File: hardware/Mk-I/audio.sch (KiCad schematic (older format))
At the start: 9 parts, among them U5 SGTL5000

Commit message: Cleanup schematics
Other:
- moved on the sheet: C10, C11, HP_OUT1, LINE_IN1, U5
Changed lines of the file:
@@
 Comment4 ""
 $EndDescr
-Text GLabel 5150 2900 0    60   Input ~ 0
+Text GLabel 4500 3300 0    60   Input ~ 0
 Audio_SDA
-Text GLabel 5150 3050 0    60   Input ~ 0
+Text GLabel 4500 3450 0    60   Input ~ 0
 Audio_SCL
-Text GLabel 5150 3300 0    60   Input ~ 0
+Text GLabel 4500 3700 0    60   Input ~ 0
 I2S_MCLK
-Text GLabel 5150 3450 0    60   Input ~ 0
+Text GLabel 4500 3850 0    60   Input ~ 0
 I2S_SCLK
-Text GLabel 5150 3600 0    60   Input ~ 0
+Text GLabel 4500 4000 0    60   Input ~ 0
 I2S_LRCLK
-Text GLabel 5150 3750 0    60   Input ~ 0
+Text GLabel 4500 4150 0    60   Input ~ 0
 I2S_DIN
-Text GLabel 5150 3900 0    60   Input ~ 0
+Text GLabel 4500 4300 0    60   Input ~ 0
 I2S_DOUT
-Text GLabel 5250 2050 0    60   Input ~ 0
+Text GLabel 4600 2450 0    60   Input ~ 0
 3V3
 Wire Wire Line
-	5150 4250 5100 4250
+	4500 4650 4450 4650
 Wire Wire Line
-	5100 4250 5100 4450
+	4450 4650 4450 4850
 $Comp
 L GND #PWR032
 U 1 1 585E79AD
-P 5100 4450
-F 0 "#PWR032" H 5100 4450 30  0001 C CNN
-F 1 "GND" H 5100 4380 30  0001 C CNN
-F 2 "" H 5100 4450 60  0001 C CNN
-F 3 "" H 5100 4450 60  0001 C CNN
-	1    5100 4450
+P 4450 4850
+F 0 "#PWR032" H 4450 4850 30  0001 C CNN
+F 1 "GND" H 4450 4780 30  0001 C CNN
+F 2 "" H 4450 4850 60  0001 C CNN
+F 3 "" H 4450 4850 60  0001 C CNN
+	1    4450 4850
 	1    0    0    -1
 $EndComp
@@
 L C C6
 U 1 1 585E7B78
-P 4750 4300
-F 0 "C6" H 4750 4400 40  0000 L CNN
-F 1 "0.1uF" H 4756 4215 40  0000 L CNN
-F 2 "Capacitors_SMD:C_0805" H 4788 4150 30  0001 C CNN
-F 3 "" H 4750 4300 60  0000 C CNN
-	1    4750 4300
+P 4100 4700
+F 0 "C6" H 4100 4800 40  0000 L CNN
+F 1 "0.1uF" H 4106 4615 40  0000 L CNN
+F 2 "Capacitors_SMD:C_0805" H 4138 4550 30  0001 C CNN
+F 3 "" H 4100 4700 60  0000 C CNN
+	1    4100 4700
 	1    0    0    -1
 $EndComp
@@
 L GND #PWR033
 U 1 1 585E7BA3
-P 4750 4500
-F 0 "#PWR033" H 4750 4500 30  0001 C CNN
-F 1 "GND" H 4750 4430 30  0001 C CNN
-F 2 "" H 4750 4500 60  0001 C CNN
-F 3 "" H 4750 4500 60  0001 C CNN
-	1    4750 4500
+P 4100 4900
+F 0 "#PWR033" H 4100 4900 30  0001 C CNN
+F 1 "GND" H 4100 4830 30  0001 C CNN
+F 2 "" H 4100 4900 60  0001 C CNN
+F 3 "" H 4100 4900 60  0001 C CNN
+	1    4100 4900
 	1    0    0    -1
 $EndComp
 Wire Wire Line
-	5150 4100 4750 4100
+	4500 4500 4100 4500
 Wire Wire Line
-	6400 3500 7375 3500
+	5750 3900 6725 3900
 Wire Wire Line
-	6400 3650 7375 3650
+	5750 4050 6725 4050
 $Comp
 L C C7
 U 1 1 585E8504
-P 5550 2300
-F 0 "C7" H 5550 2400 40  0000 L CNN
-F 1 "0.1uF" H 5556 2215 40  0000 L CNN
-F 2 "Capacitors_SMD:C_0805" H 5588 2150 30  0001 C CNN
-F 3 "" H 5550 2300 60  0000 C CNN
-	1    5550 2300
+P 4900 2700
+F 0 "C7" H 4900 2800 40  0000 L CNN
+F 1 "0.1uF" H 4906 2615 40  0000 L CNN
+F 2 "Capacitors_SMD:C_0805" H 4938 2550 30  0001 C CNN
+F 3 "" H 4900 2700 60  0000 C CNN
+	1    4900 2700
 	1    0    0    -1
 $EndComp
@@
 L C C8
 U 1 1 585E857A
-P 5800 2300
-F 0 "C8" H 5800 2400 40  0000 L CNN
-F 1 "0.1uF" H 5806 2215 40  0000 L CNN
-F 2 "Capacitors_SMD:C_0805" H 5838 2150 30  0001 C CNN
-F 3 "" H 5800 2300 60  0000 C CNN
-	1    5800 2300
+P 5150 2700
+F 0 "C8" H 5150 2800 40  0000 L CNN
+F 1 "0.1uF" H 5156 2615 40  0000 L CNN
+F 2 "Capacitors_SMD:C_0805" H 5188 2550 30  0001 C CNN
+F 3 "" H 5150 2700 60  0000 C CNN
+	1    5150 2700
 	1    0    0    -1
 $EndComp
@@
 L C C9
 U 1 1 585E859F
-P 6050 2300
-F 0 "C9" H 6050 2400 40  0000 L CNN
-F 1 "0.1uF" H 6056 2215 40  0000 L CNN
-F 2 "Capacitors_SMD:C_0805" H 6088 2150 30  0001 C CNN
-F 3 "" H 6050 2300 60  0000 C CNN
-	1    6050 2300
+P 5400 2700
+F 0 "C9" H 5400 2800 40  0000 L CNN
+F 1 "0.1uF" H 5406 2615 40  0000 L CNN
+F 2 "Capacitors_SMD:C_0805" H 5438 2550 30  0001 C CNN
+F 3 "" H 5400 2700 60  0000 C CNN
+	1    5400 2700
 	1    0    0    -1
 $EndComp
@@
 L SGTL5000 U5
 U 1 1 585E883F
-P 5400 2800
-F 0 "U5" H 5300 3050 60  0000 C CNN
-F 1 "SGTL5000" H 5750 1250 60  0000 C CNN
-F 2 "Housings_DFN_QFN:UQFN-20-1EP_3x3mm_Pitch0.4mm" H 5400 2750 60  0001 C CNN
-F 3 "" H 5400 2750 60  0001 C CNN
-	1    5400 2800
+P 4750 3200
+F 0 "U5" H 4650 3450 60  0000 C CNN
+F 1 "SGTL5000" H 5100 1650 60  0000 C CNN
+F 2 "Housings_DFN_QFN:UQFN-20-1EP_3x3mm_Pitch0.4mm" H 4750 3150 60  0001 C CNN
+F 3 "" H 4750 3150 60  0001 C CNN
+	1    4750 3200
 	1    0    0    -1
 $EndComp
 Wire Wire Line
-	6050 2100 6050 2050
+	5400 2500 5400 2450
 Wire Wire Line
-	6050 2050 5250 2050
+	5400 2450 4600 2450
 Wire Wire Line
-	5550 2100 5550 2050
-Connection ~ 5550 2050
+	4900 2500 4900 2450
+Connection ~ 4900 2450
 Wire Wire Line
-	5800 2100 5800 2050
-Connection ~ 5800 2050
+	5150 2500 5150 2450
+Connection ~ 5150 2450
 $Comp
 L Csmall C10
 U 1 1 585E8C6B
-P 6650 2900
-F 0 "C10" V 6700 2800 30  0000 L CNN
-F 1 "1uF" V 6700 2950 30  0000 L CNN
-F 2 "Capacitors_SMD:C_0805" H 6650 2900 60  0001 C CNN
-F 3 "" H 6650 2900 60  0000 C CNN
-	1    6650 2900
+P 6000 3300
+F 0 "C10" V 6050 3200 30  0000 L CNN
+F 1 "1uF" V 6050 3350 30  0000 L CNN
+F 2 "Capacitors_SMD:C_0805" H 6000 3300 60  0001 C CNN
+F 3 "" H 6000 3300 60  0000 C CNN
+	1    6000 3300
 	0    1    1    0
 $EndComp
@@
 L Csmall C11
 U 1 1 585E8E3F
-P 6650 3050
-F 0 "C11" V 6700 2950 30  0000 L CNN
-F 1 "1uF" V 6700 3100 30  0000 L CNN
-F 2 "Capacitors_SMD:C_0805" H 6650 3050 60  0001 C CNN
-F 3 "" H 6650 3050 60  0000 C CNN
-	1    6650 3050
+P 6000 3450
+F 0 "C11" V 6050 3350 30  0000 L CNN
+F 1 "1uF" V 6050 3500 30  0000 L CNN
+F 2 "Capacitors_SMD:C_0805" H 6000 3450 60  0001 C CNN
+F 3 "" H 6000 3450 60  0000 C CNN
+	1    6000 3450
 	0    1    1    0
 $EndComp
 Wire Wire Line
-	6550 2900 6400 2900
+	5900 3300 5750 3300
 Wire Wire Line
-	6550 3050 6400 3050
+	5900 3450 5750 3450
 Wire Wire Line
-	6750 2900 7375 2900
+	6100 3300 6725 3300
 Wire Wire Line
-	6750 3050 7375 3050
+	6100 3450 6725 3450
 $Comp
 L 3.5_audio_jack HP_OUT1
 U 1 1 5863AC9E
-P 7750 4025
-F 0 "HP_OUT1" H 7825 3400 60  0000 C CNN
-F 1 "3.5_audio_jack" H 7750 4025 60  0001 C CNN
-F 2 "POSS:lumberg_3.5_audio_jack_1503_02" H 7750 4025 60  0001 C CNN
-F 3 "" H 7750 4025 60  0001 C CNN
-	1    7750 4025
+P 7100 4425
+F 0 "HP_OUT1" H 7175 3800 60  0000 C CNN
+F 1 "3.5_audio_jack" H 7100 4425 60  0001 C CNN
+F 2 "POSS:lumberg_3.5_audio_jack_1503_02" H 7100 4425 60  0001 C CNN
+F 3 "" H 7100 4425 60  0001 C CNN
+	1    7100 4425
 	-1   0    0    1
 $EndComp
 Wire Wire Line
-	6400 3800 7375 3800
+	5750 4200 6725 4200
 $Comp
 L 3.5_audio_jack LINE_IN1
 U 1 1 5863B129
-P 7750 3425
-F 0 "LINE_IN1" H 7825 2800 60  0000 C CNN
-F 1 "3.5_audio_jack" H 7600 2800 60  0001 C CNN
-F 2 "POSS:lumberg_3.5_audio_jack_1503_02" H 7750 3425 60  0001 C CNN
-F 3 "" H 7750 3425 60  0001 C CNN
-	1    7750 3425
+P 7100 3825
+F 0 "LINE_IN1" H 7175 3200 60  0000 C CNN
+F 1 "3.5_audio_jack" H 6950 3200 60  0001 C CNN
+F 2 "POSS:lumberg_3.5_audio_jack_1503_02" H 7100 3825 60  0001 C CNN
+F 3 "" H 7100 3825 60  0001 C CNN
+	1    7100 3825
 	-1   0    0    1
 $EndComp
@@
 L GND #PWR034
 U 1 1 5863B3F7
-P 7325 3275
-F 0 "#PWR034" H 7325 3275 30  0001 C CNN
-F 1 "GND" H 7325 3205 30  0001 C CNN
-F 2 "" H 7325 3275 60  0001 C CNN
-F 3 "" H 7325 3275 60  0001 C CNN
-	1    7325 3275
+P 6675 3675
+F 0 "#PWR034" H 6675 3675 30  0001 C CNN
+F 1 "GND" H 6675 3605 30  0001 C CNN
+F 2 "" H 6675 3675 60  0001 C CNN
+F 3 "" H 6675 3675 60  0001 C CNN
+	1    6675 3675
 	1    0    0    -1
 $EndComp
 Wire Wire Line
-	7375 3200 7325 3200
+	6725 3600 6675 3600
 Wire Wire Line
-	7325 3200 7325 3275
+	6675 3600 6675 3675
 $EndSCHEMATC

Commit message: HW: Add a DFU mode switch
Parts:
- C6, C7, C8, C9: symbol C -> C-RESCUE-wnm_mk_1
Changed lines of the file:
@@
 EESchema Schematic File Version 2
+LIBS:wnm_mk_1-rescue
 LIBS:power
 LIBS:device
@@
 LIBS:microchip_pic12mcu
 LIBS:microchip_pic16mcu
-LIBS:microchip1
 LIBS:msp430
 LIBS:nxp_armmcu
@@
 LIBS:relays
 LIBS:sensors
-LIBS:special
 LIBS:stm8
 LIBS:stm32
@@
 	4450 4650 4450 4850
 $Comp
-L GND #PWR032
+L GND-RESCUE-wnm_mk_1 #PWR032
 U 1 1 585E79AD
 P 4450 4850
+AR Path="/585E79AD" Ref="#PWR032"  Part="1"
+AR Path="/585E4C2D/585E79AD" Ref="#PWR032"  Part="1"
 F 0 "#PWR032" H 4450 4850 30  0001 C CNN
 F 1 "GND" H 4450 4780 30  0001 C CNN
@@
 $EndComp
 $Comp
-L C C6
+L C-RESCUE-wnm_mk_1 C6
 U 1 1 585E7B78
 P 4100 4700
+AR Path="/585E7B78" Ref="C6"  Part="1"
+AR Path="/585E4C2D/585E7B78" Ref="C6"  Part="1"
 F 0 "C6" H 4100 4800 40  0000 L CNN
 F 1 "0.1uF" H 4106 4615 40  0000 L CNN
@@
 $EndComp
 $Comp
-L GND #PWR033
+L GND-RESCUE-wnm_mk_1 #PWR033
 U 1 1 585E7BA3
 P 4100 4900
+AR Path="/585E7BA3" Ref="#PWR033"  Part="1"
+AR Path="/585E4C2D/585E7BA3" Ref="#PWR033"  Part="1"
 F 0 "#PWR033" H 4100 4900 30  0001 C CNN
 F 1 "GND" H 4100 4830 30  0001 C CNN
@@
 	5750 4050 6725 4050
 $Comp
-L C C7
+L C-RESCUE-wnm_mk_1 C7
 U 1 1 585E8504
 P 4900 2700
+AR Path="/585E8504" Ref="C7"  Part="1"
+AR Path="/585E4C2D/585E8504" Ref="C7"  Part="1"
 F 0 "C7" H 4900 2800 40  0000 L CNN
 F 1 "0.1uF" H 4906 2615 40  0000 L CNN
@@
 $EndComp
 $Comp
-L C C8
+L C-RESCUE-wnm_mk_1 C8
 U 1 1 585E857A
 P 5150 2700
+AR Path="/585E857A" Ref="C8"  Part="1"
+AR Path="/585E4C2D/585E857A" Ref="C8"  Part="1"
 F 0 "C8" H 5150 2800 40  0000 L CNN
 F 1 "0.1uF" H 5156 2615 40  0000 L CNN
@@
 $EndComp
 $Comp
-L C C9
+L C-RESCUE-wnm_mk_1 C9
 U 1 1 585E859F
 P 5400 2700
+AR Path="/585E859F" Ref="C9"  Part="1"
+AR Path="/585E4C2D/585E859F" Ref="C9"  Part="1"
 F 0 "C9" H 5400 2800 40  0000 L CNN
 F 1 "0.1uF" H 5406 2615 40  0000 L CNN
@@
 $EndComp
 $Comp
-L GND #PWR034
+L GND-RESCUE-wnm_mk_1 #PWR034
 U 1 1 5863B3F7
 P 6675 3675
+AR Path="/5863B3F7" Ref="#PWR034"  Part="1"
+AR Path="/585E4C2D/5863B3F7" Ref="#PWR034"  Part="1"
 F 0 "#PWR034" H 6675 3675 30  0001 C CNN
 F 1 "GND" H 6675 3605 30  0001 C CNN

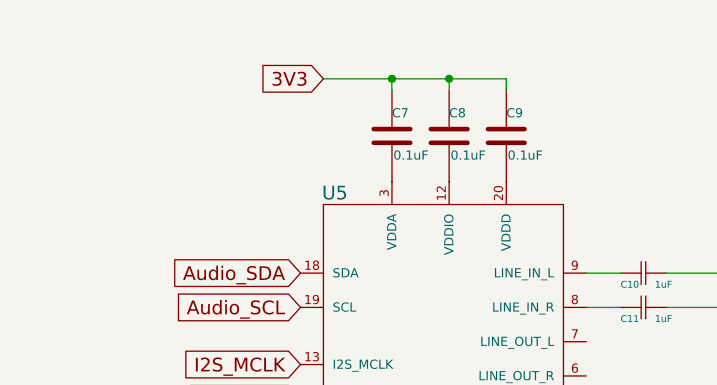
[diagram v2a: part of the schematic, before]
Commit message: HW: Fix DAC coupling caps
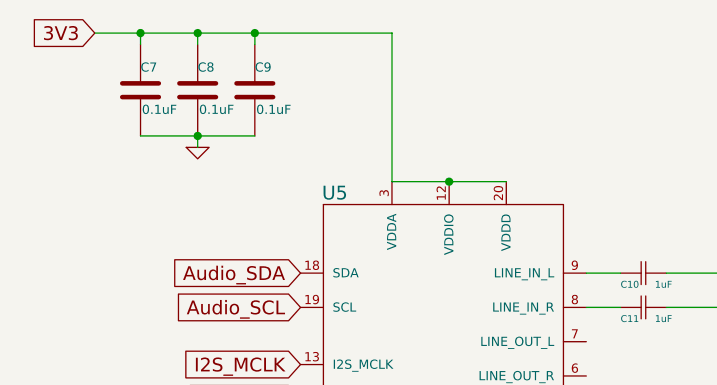
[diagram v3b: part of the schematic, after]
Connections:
- net 3V3: now also U5.12 (VDDIO), U5.20 (VDDD), U5.3 (VDDA)
- net GND: now also C7.2, C8.2, C9.2
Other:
- moved on the sheet: C7, C8, C9
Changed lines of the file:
@@
 Text GLabel 4500 4300 0    60   Input ~ 0
 I2S_DOUT
-Text GLabel 4600 2450 0    60   Input ~ 0
+Text GLabel 3600 2250 0    60   Input ~ 0
 3V3
 Wire Wire Line
@@
 L C-RESCUE-wnm_mk_1 C7
 U 1 1 585E8504
-P 4900 2700
+P 3800 2500
 AR Path="/585E8504" Ref="C7"  Part="1"
 AR Path="/585E4C2D/585E8504" Ref="C7"  Part="1"
-F 0 "C7" H 4900 2800 40  0000 L CNN
-F 1 "0.1uF" H 4906 2615 40  0000 L CNN
-F 2 "Capacitors_SMD:C_0805" H 4938 2550 30  0001 C CNN
-F 3 "" H 4900 2700 60  0000 C CNN
-	1    4900 2700
+F 0 "C7" H 3800 2600 40  0000 L CNN
+F 1 "0.1uF" H 3806 2415 40  0000 L CNN
+F 2 "Capacitors_SMD:C_0805" H 3838 2350 30  0001 C CNN
+F 3 "" H 3800 2500 60  0000 C CNN
+	1    3800 2500
 	1    0    0    -1
 $EndComp
@@
 L C-RESCUE-wnm_mk_1 C8
 U 1 1 585E857A
-P 5150 2700
+P 4050 2500
 AR Path="/585E857A" Ref="C8"  Part="1"
 AR Path="/585E4C2D/585E857A" Ref="C8"  Part="1"
-F 0 "C8" H 5150 2800 40  0000 L CNN
-F 1 "0.1uF" H 5156 2615 40  0000 L CNN
-F 2 "Capacitors_SMD:C_0805" H 5188 2550 30  0001 C CNN
-F 3 "" H 5150 2700 60  0000 C CNN
-	1    5150 2700
+F 0 "C8" H 4050 2600 40  0000 L CNN
+F 1 "0.1uF" H 4056 2415 40  0000 L CNN
+F 2 "Capacitors_SMD:C_0805" H 4088 2350 30  0001 C CNN
+F 3 "" H 4050 2500 60  0000 C CNN
+	1    4050 2500
 	1    0    0    -1
 $EndComp
@@
 L C-RESCUE-wnm_mk_1 C9
 U 1 1 585E859F
-P 5400 2700
+P 4300 2500
 AR Path="/585E859F" Ref="C9"  Part="1"
 AR Path="/585E4C2D/585E859F" Ref="C9"  Part="1"
-F 0 "C9" H 5400 2800 40  0000 L CNN
-F 1 "0.1uF" H 5406 2615 40  0000 L CNN
-F 2 "Capacitors_SMD:C_0805" H 5438 2550 30  0001 C CNN
-F 3 "" H 5400 2700 60  0000 C CNN
-	1    5400 2700
+F 0 "C9" H 4300 2600 40  0000 L CNN
+F 1 "0.1uF" H 4306 2415 40  0000 L CNN
+F 2 "Capacitors_SMD:C_0805" H 4338 2350 30  0001 C CNN
+F 3 "" H 4300 2500 60  0000 C CNN
+	1    4300 2500
 	1    0    0    -1
 $EndComp
@@
 $EndComp
 Wire Wire Line
-	5400 2500 5400 2450
-Wire Wire Line
-	5400 2450 4600 2450
-Wire Wire Line
-	4900 2500 4900 2450
-Connection ~ 4900 2450
-Wire Wire Line
-	5150 2500 5150 2450
-Connection ~ 5150 2450
+	4300 2250 4300 2300
+Wire Wire Line
+	3800 2300 3800 2250
+Connection ~ 3800 2250
+Wire Wire Line
+	4050 2250 4050 2300
+Connection ~ 4050 2250
 $Comp
 L Csmall C10
@@
 Wire Wire Line
 	6675 3600 6675 3675
+Wire Wire Line
+	3600 2250 4900 2250
+Wire Wire Line
+	4900 2250 4900 2900
+Connection ~ 4300 2250
+Wire Wire Line
+	4900 2900 5400 2900
+Connection ~ 5150 2900
+Wire Wire Line
+	3800 2700 4300 2700
+Connection ~ 4050 2700
+$Comp
+L GND-RESCUE-wnm_mk_1 #PWR035
+U 1 1 58BC5E4F
+P 4050 2750
+F 0 "#PWR035" H 4050 2750 30  0001 C CNN
+F 1 "GND" H 4050 2680 30  0001 C CNN
+F 2 "" H 4050 2750 60  0001 C CNN
+F 3 "" H 4050 2750 60  0001 C CNN
+	1    4050 2750
+	1    0    0    -1
+$EndComp
+Wire Wire Line
+	4050 2750 4050 2700
 $EndSCHEMATC

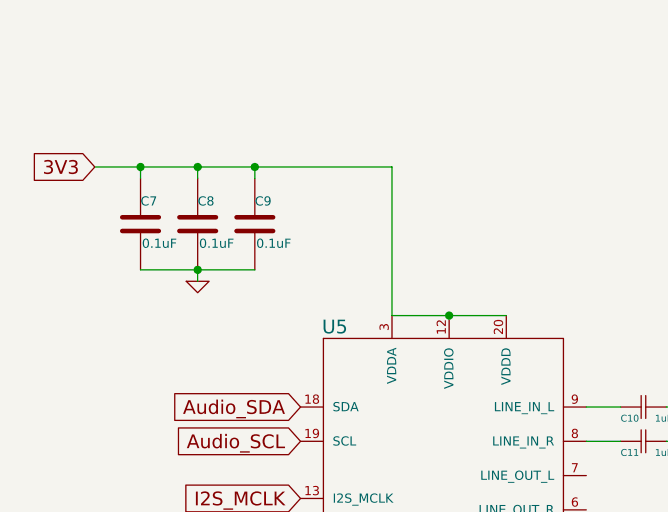
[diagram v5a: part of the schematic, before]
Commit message: HW: Start rev-C with DAC VDDD fix
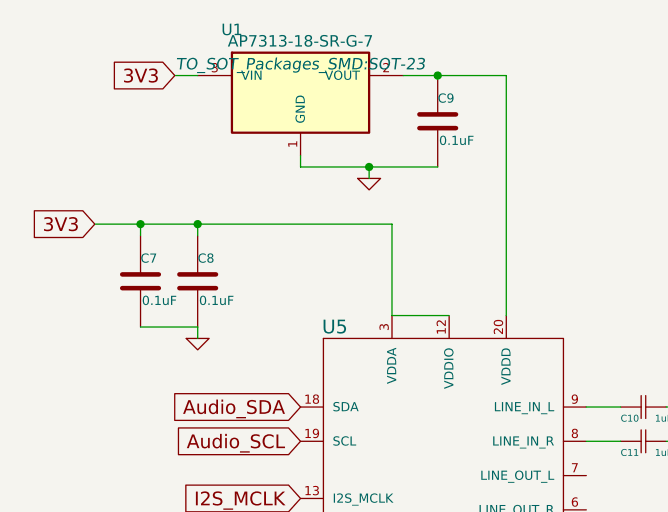
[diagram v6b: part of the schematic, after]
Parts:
- added U1: AP7313-18-SR-G-7, TO_SOT_Packages_SMD:SOT-23, symbol APE8865N-18-HF-3
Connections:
- net 3V3: now also U1.3 (VIN); no longer C9.1, U5.20 (VDDD)
- net GND: now also U1.1 (GND)
- new net: C9.1, U1.2 (VOUT), U5.20 (VDDD)
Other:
- moved on the sheet: C7, C8, C9
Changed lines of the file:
@@
 Title "Wee Noise Maker - Mk-I"
 Date ""
-Rev "B"
+Rev "C"
 Comp "Fabien Chouteau"
 Comment1 ""
@@
 Text GLabel 4500 4300 0    60   Input ~ 0
 I2S_DOUT
-Text GLabel 3600 2250 0    60   Input ~ 0
+Text GLabel 3600 2500 0    60   Input ~ 0
 3V3
 Wire Wire Line
@@
 L C-RESCUE-wnm_mk_1 C7
 U 1 1 585E8504
-P 3800 2500
+P 3800 2750
 AR Path="/585E8504" Ref="C7"  Part="1"
 AR Path="/585E4C2D/585E8504" Ref="C7"  Part="1"
-F 0 "C7" H 3800 2600 40  0000 L CNN
-F 1 "0.1uF" H 3806 2415 40  0000 L CNN
-F 2 "Capacitors_SMD:C_0805" H 3838 2350 30  0001 C CNN
-F 3 "" H 3800 2500 60  0000 C CNN
-	1    3800 2500
+F 0 "C7" H 3800 2850 40  0000 L CNN
+F 1 "0.1uF" H 3806 2665 40  0000 L CNN
+F 2 "Capacitors_SMD:C_0805" H 3838 2600 30  0001 C CNN
+F 3 "" H 3800 2750 60  0000 C CNN
+	1    3800 2750
 	1    0    0    -1
 $EndComp
@@
 L C-RESCUE-wnm_mk_1 C8
 U 1 1 585E857A
-P 4050 2500
+P 4050 2750
 AR Path="/585E857A" Ref="C8"  Part="1"
 AR Path="/585E4C2D/585E857A" Ref="C8"  Part="1"
-F 0 "C8" H 4050 2600 40  0000 L CNN
-F 1 "0.1uF" H 4056 2415 40  0000 L CNN
-F 2 "Capacitors_SMD:C_0805" H 4088 2350 30  0001 C CNN
-F 3 "" H 4050 2500 60  0000 C CNN
-	1    4050 2500
+F 0 "C8" H 4050 2850 40  0000 L CNN
+F 1 "0.1uF" H 4056 2665 40  0000 L CNN
+F 2 "Capacitors_SMD:C_0805" H 4088 2600 30  0001 C CNN
+F 3 "" H 4050 2750 60  0000 C CNN
+	1    4050 2750
 	1    0    0    -1
 $EndComp
@@
 L C-RESCUE-wnm_mk_1 C9
 U 1 1 585E859F
-P 4300 2500
+P 5100 2050
 AR Path="/585E859F" Ref="C9"  Part="1"
 AR Path="/585E4C2D/585E859F" Ref="C9"  Part="1"
-F 0 "C9" H 4300 2600 40  0000 L CNN
-F 1 "0.1uF" H 4306 2415 40  0000 L CNN
-F 2 "Capacitors_SMD:C_0805" H 4338 2350 30  0001 C CNN
-F 3 "" H 4300 2500 60  0000 C CNN
-	1    4300 2500
+F 0 "C9" H 5100 2150 40  0000 L CNN
+F 1 "0.1uF" H 5106 1965 40  0000 L CNN
+F 2 "Capacitors_SMD:C_0805" H 5138 1900 30  0001 C CNN
+F 3 "" H 5100 2050 60  0000 C CNN
+	1    5100 2050
 	1    0    0    -1
 $EndComp
@@
 $EndComp
 Wire Wire Line
-	4300 2250 4300 2300
-Wire Wire Line
-	3800 2300 3800 2250
-Connection ~ 3800 2250
-Wire Wire Line
-	4050 2250 4050 2300
-Connection ~ 4050 2250
+	3800 2550 3800 2500
+Connection ~ 3800 2500
+Wire Wire Line
+	4050 2500 4050 2550
+Connection ~ 4050 2500
 $Comp
 L Csmall C10
@@
 	6675 3600 6675 3675
 Wire Wire Line
-	3600 2250 4900 2250
-Wire Wire Line
-	4900 2250 4900 2900
-Connection ~ 4300 2250
-Wire Wire Line
-	4900 2900 5400 2900
-Connection ~ 5150 2900
-Wire Wire Line
-	3800 2700 4300 2700
-Connection ~ 4050 2700
+	3600 2500 4900 2500
 $Comp
 L GND-RESCUE-wnm_mk_1 #PWR036
 U 1 1 58BC5E4F
-P 4050 2750
-F 0 "#PWR036" H 4050 2750 30  0001 C CNN
-F 1 "GND" H 4050 2680 30  0001 C CNN
-F 2 "" H 4050 2750 60  0001 C CNN
-F 3 "" H 4050 2750 60  0001 C CNN
-	1    4050 2750
-	1    0    0    -1
-$EndComp
-Wire Wire Line
-	4050 2750 4050 2700
+P 4050 3000
+F 0 "#PWR036" H 4050 3000 30  0001 C CNN
+F 1 "GND" H 4050 2930 30  0001 C CNN
+F 2 "" H 4050 3000 60  0001 C CNN
+F 3 "" H 4050 3000 60  0001 C CNN
+	1    4050 3000
+	1    0    0    -1
+$EndComp
+$Comp
+L APE8865N-18-HF-3 U1
+U 1 1 58E3EC1A
+P 4500 1900
+F 0 "U1" H 4200 2150 50  0000 C CNN
+F 1 "AP7313-18-SR-G-7" H 4500 2100 50  0000 C CNN
+F 2 "TO_SOT_Packages_SMD:SOT-23" H 4500 2000 50  0000 C CIN
+F 3 "" H 4500 1900 50  0000 C CNN
+	1    4500 1900
+	1    0    0    -1
+$EndComp
+Wire Wire Line
+	4900 2900 5150 2900
+Wire Wire Line
+	4900 2500 4900 2900
+Wire Wire Line
+	3800 2950 4050 2950
+Wire Wire Line
+	4050 2950 4050 3000
+Text GLabel 3950 1850 0    60   Input ~ 0
+3V3
+Wire Wire Line
+	3950 1850 4050 1850
+Wire Wire Line
+	4950 1850 5400 1850
+Wire Wire Line
+	5400 1850 5400 2900
+Connection ~ 5100 1850
+Wire Wire Line
+	5100 2250 4500 2250
+Wire Wire Line
+	4500 2250 4500 2200
+$Comp
+L GND-RESCUE-wnm_mk_1 #PWR037
+U 1 1 58E3F7FA
+P 4800 2300
+F 0 "#PWR037" H 4800 2300 30  0001 C CNN
+F 1 "GND" H 4800 2230 30  0001 C CNN
+F 2 "" H 4800 2300 60  0001 C CNN
+F 3 "" H 4800 2300 60  0001 C CNN
+	1    4800 2300
+	1    0    0    -1
+$EndComp
+Wire Wire Line
+	4800 2300 4800 2250
+Connection ~ 4800 2250
 $EndSCHEMATC
